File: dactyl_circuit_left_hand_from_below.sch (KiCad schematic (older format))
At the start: 154 parts

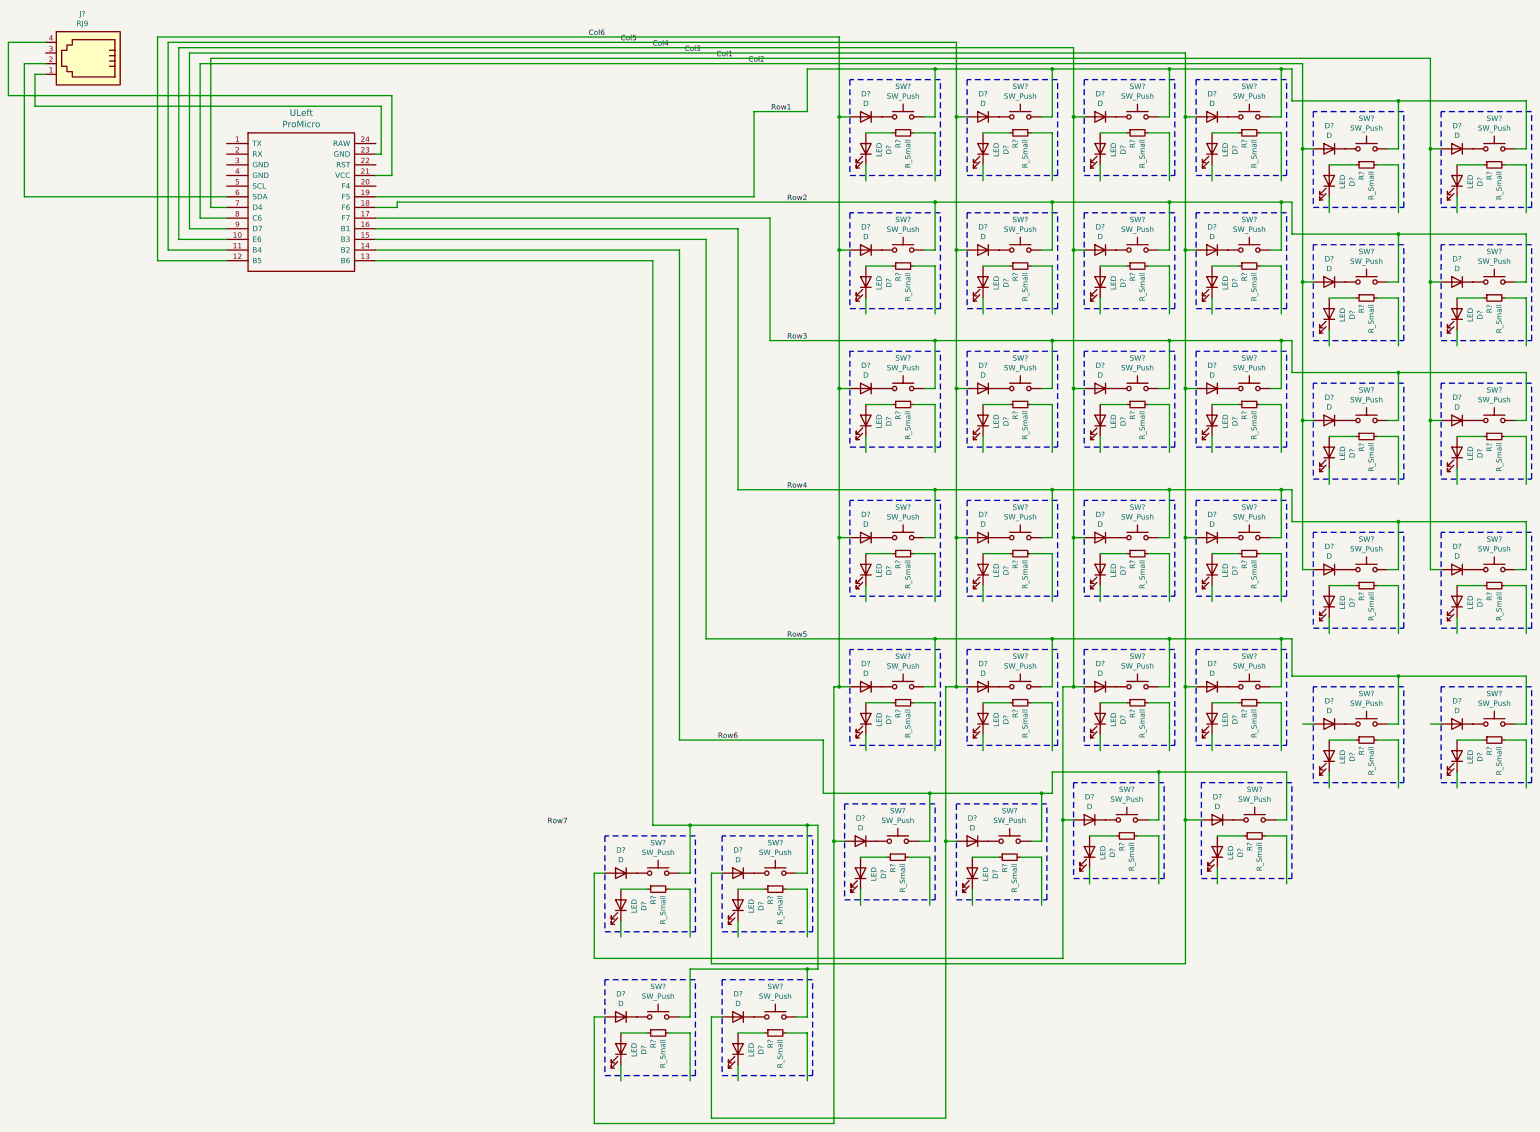
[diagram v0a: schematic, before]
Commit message: Wiring : redo the matrix properly to follow qmk_firmware. Diode placement within switch to be checked
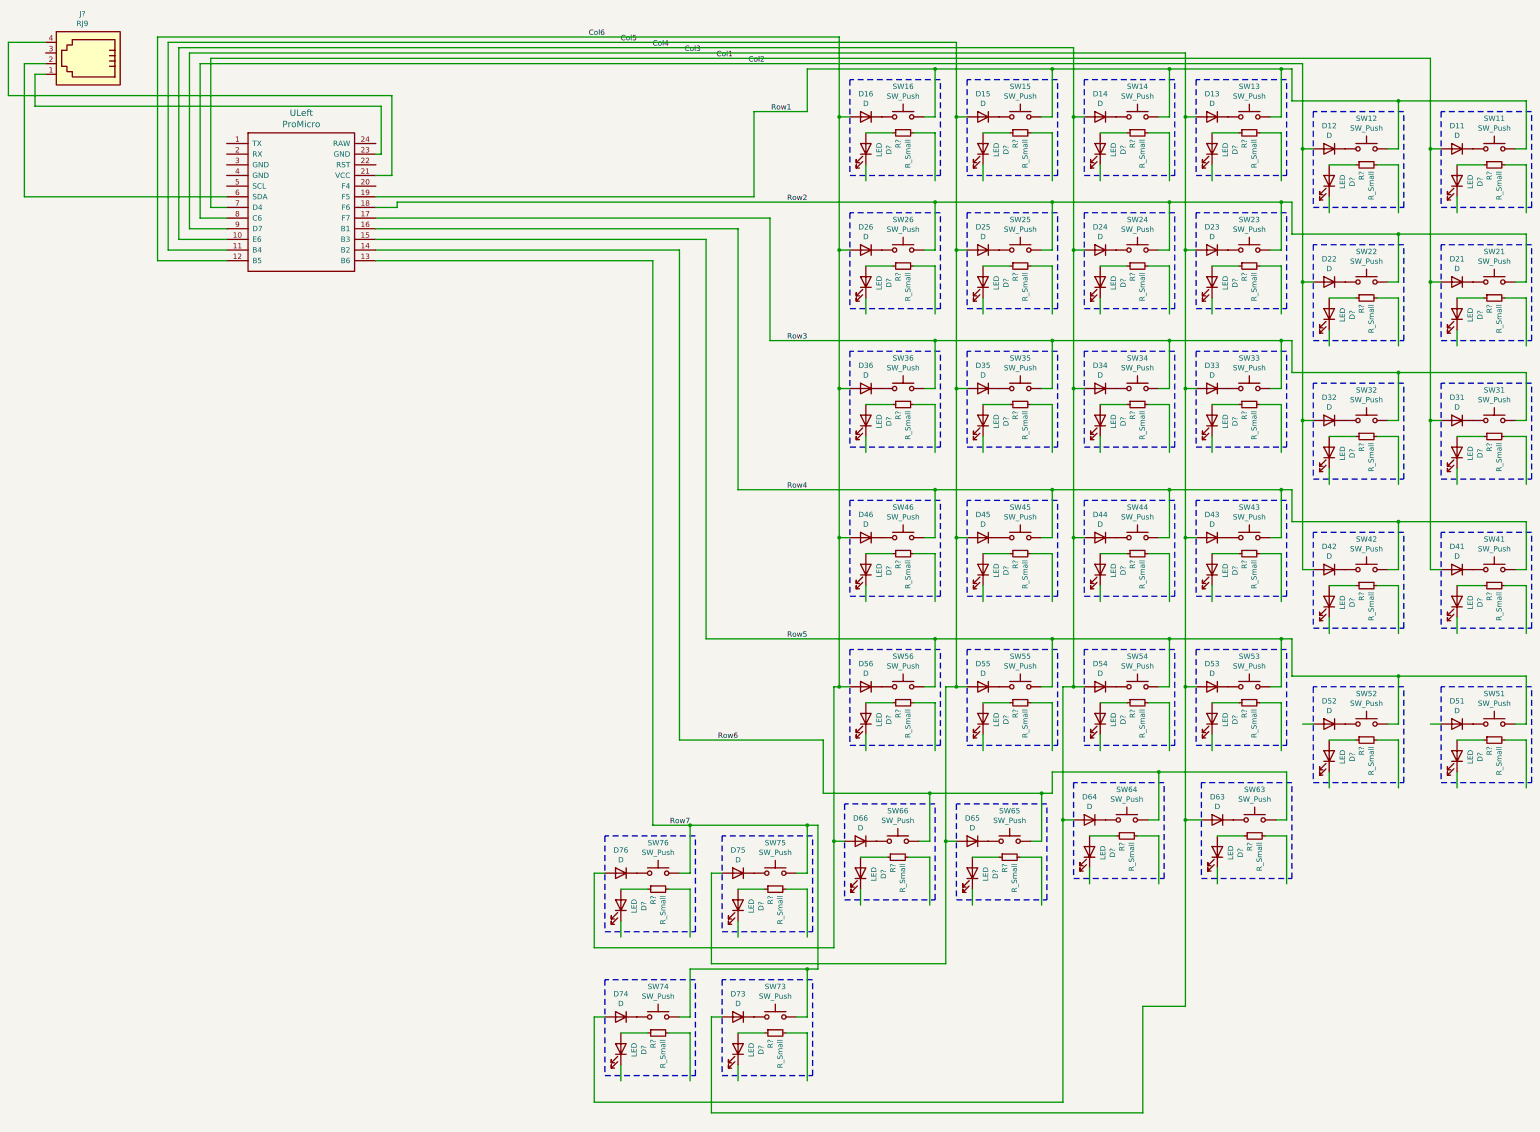
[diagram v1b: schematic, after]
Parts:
- gave numbers to parts that had none: 76
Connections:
- wire segments 414 -> 416
